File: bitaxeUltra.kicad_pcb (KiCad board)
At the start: 4 copper layers, 56.5 x 99.8 mm, 137 parts, among them J1 54-00164, J2 Conn_01x02, J3 Conn_01x05, J4 Conn_01x04, J5 TC2030-IDC, J7 Conn_01x02, J8 USB_C_Receptacle_USB2.0, J9 Conn_01x04, Q1 CSD17311Q5, Q2 CSD17311Q5, Q4 2N7002K, SW1 GT-TC029B-H025-L1N, SW2 GT-TC029B-H025-L1N, U1 25MHz, U10 DS4432U+, U11 RT9080-33GJ5, U12 ESP32-S3-WROOM-1, U14 BM1366_mode1, U2 TXB0104RGYR, U5 MCP1824T-1802E, U6 MCP1824T-0802E, U7 EMC2101, U8 INA260, U9 TPS40305, Y1 32.768kHz

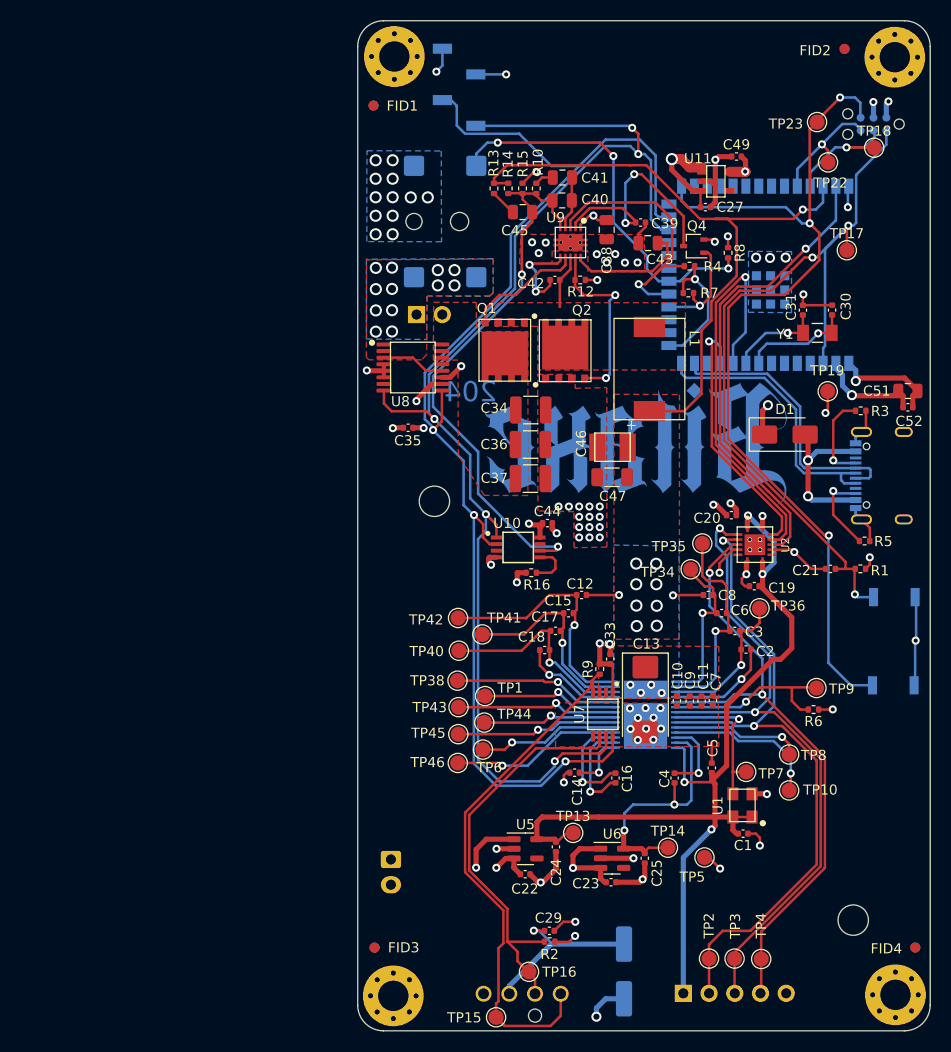
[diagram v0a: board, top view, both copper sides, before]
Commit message: Power analysis; updates to 205pd
Started analysis based on the 204 with an architecture diagram and with an smath document. Copied over manually changes from the 205 branch and started updating the schematic with USB PD capabilities. Only added decoy USB PD chip (CH224K), still need to fix power supplies.
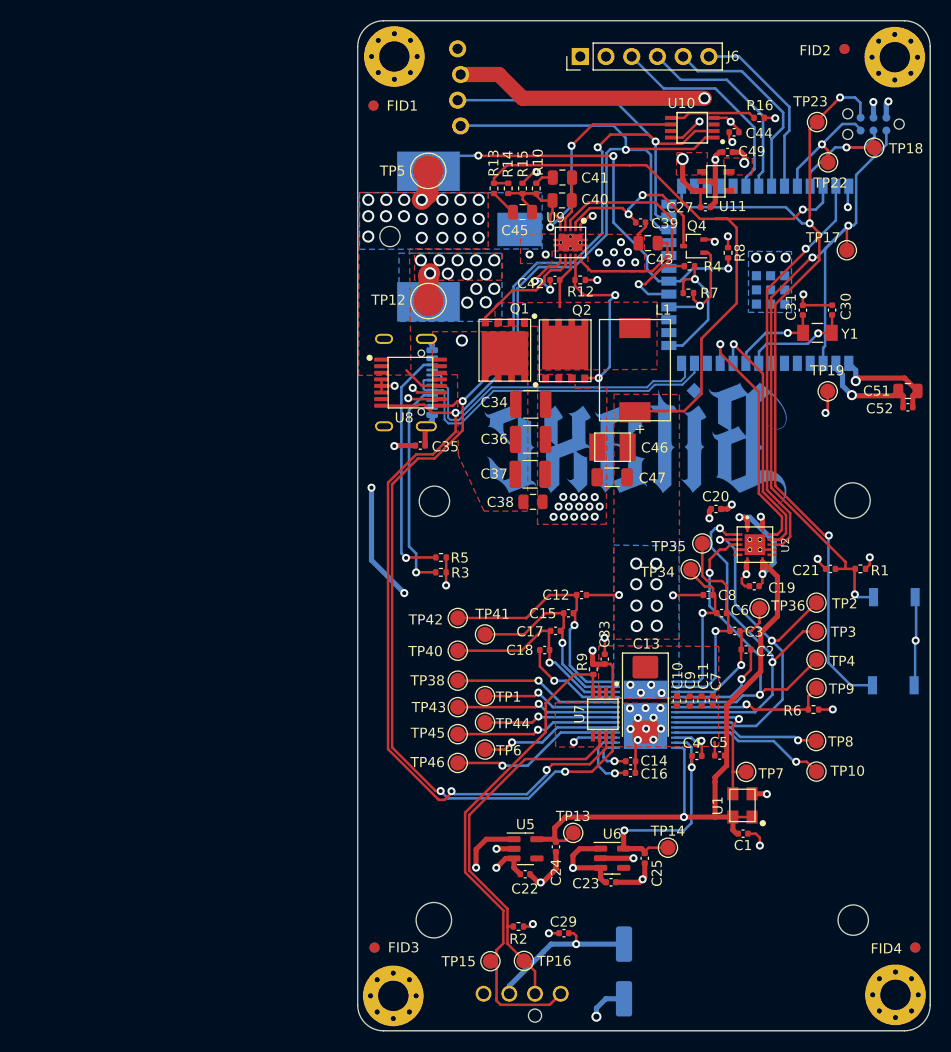
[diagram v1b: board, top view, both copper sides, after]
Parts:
- removed D1: SS310, Diode_SMD:D_SMA
- removed J2: Conn_01x02, bitaxe:JST_XH_B2B-XH-A_1x02_P2.50mm_Vertical
- removed J3: Conn_01x05, Connector_PinHeader_2.54mm:PinHeader_1x05_P2.54mm_Vertical
- removed J7: Conn_01x02, Connector_PinHeader_2.54mm:PinHeader_1x02_P2.54mm_Vertical
- added H1: MountingHole, MountingHole:MountingHole_3.5mm, F.Cu at (126.1, 94.9)
- added H2: MountingHole, MountingHole:MountingHole_3.5mm, F.Cu at (84.7, 136.4)
- added J6: Conn_01x06, Connector_PinHeader_2.54mm:PinHeader_1x06_P2.54mm_Vertical, F.Cu at (99.2, 51.1)
- added TP12: TestPoint, TestPoint:TestPoint_Pad_D3.0mm, F.Cu at (84.2, 75.2)
- J1: value 54-00164 -> PJ-036AH-SMT; footprint bitaxe:BarrelJack_Wuerth_694106106102_2.0x5.5mm -> Connector_BarrelJack:BarrelJack_CUI_PJ-036AH-SMT_Horizontal
- J9: footprint Connector_PinSocket_2.54mm:PinSocket_1x04_P2.54mm_Vertical_SMD_Pin1Right -> bitaxe:PinHeader_1x04_P2.54mm_Vertical_shifted
- TP5: footprint TestPoint:TestPoint_Pad_D1.5mm -> TestPoint:TestPoint_Pad_D3.0mm
- moved TP5 73.1 mm to (84.2, 62.4)
- moved R16 50.3 mm to (116.8, 57.1), turned to 0 degrees
- moved J8 50.0 mm to (80.9, 83.3), turned to 90 degrees
- moved U10 44.9 mm to (110.2, 58.1), turned to 180 degrees
- moved R3 44.4 mm to (85.4, 102.0)
- moved C44 42.8 mm to (114.4, 58.5)
- moved R5 41.9 mm to (85.4, 100.5)
- moved TP2 36.7 mm to (122.5, 105.0)
- moved TP3 33.3 mm to (122.5, 107.8)
- moved TP4 30.0 mm to (122.5, 110.7), turned to 0 degrees
- moved C38 27.8 mm to (94.5, 95.0), turned to 0 degrees
- moved C14 5.65 mm to (104.2, 120.7), turned to 0 degrees
- moved TP15 5.57 mm to (90.3, 140.4)
- moved U3 4.21 mm to (96.7, 71.6), turned to 180 degrees
- moved J9 3.80 mm to (87.2, 50.3)
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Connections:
- net Net-(U12-GPIO19/U1RTS/ADC2_CH8/CLK_OUT2/USB_D-) renamed /ESP32/USB_D-
- net Net-(U12-GPIO20/U1CTS/ADC2_CH9/CLK_OUT1/USB_D+) renamed /ESP32/USB_D+
- J8 pad A4: Net-(D1-Pad2) -> unconnected-(J8-VBUS-PadA4)
- J8 pad B4: Net-(D1-Pad2) -> unconnected-(J8-VBUS-PadB4)
- TP5 pad 1: GND -> /Power/VIN
- U12 pad 32: unconnected-(U12-MTCK/GPIO39/CLK_OUT3/SUBSPICS1-Pad32) -> Net-(J6-Pin_3)
- U12 pad 33: unconnected-(U12-MTDO/GPIO40/CLK_OUT2-Pad33) -> Net-(J6-Pin_4)
- U12 pad 34: unconnected-(U12-MTDI/GPIO41/CLK_OUT1-Pad34) -> Net-(J6-Pin_5)
- U12 pad 35: unconnected-(U12-MTMS/GPIO42-Pad35) -> Net-(J6-Pin_6)
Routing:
- net /BM1366/CI: track 67.5 -> 38.3 mm
- net /BM1366/RO: track 66.2 -> 37.6 mm
- net /BM1366/RST_N: track 62.1 -> 34.5 mm
- net /5V: track 217.6 -> 191.9 mm
- net /Power/OUT0: track 55.9 -> 31.2 mm
- net /3V3: track 74.3 -> 98.1 mm, vias 15 -> 18
- net Net-(J6-Pin_3): track 0.00 -> 21.2 mm
- net Net-(J6-Pin_4): track 0.00 -> 20.0 mm
- net Net-(J6-Pin_5): track 0.00 -> 19.9 mm
- net /BM1366/1V8: track 94.1 -> 74.9 mm, vias 4 -> 3
- net /SDA: track 128.0 -> 147.1 mm, vias 5 -> 4
- net GND: track 148.3 -> 129.7 mm, vias 83 -> 80
- net Net-(J6-Pin_6): track 0.00 -> 18.0 mm
- net /SCL: track 126.5 -> 143.3 mm, vias 3 -> 5
- net Net-(D1-Pad2): track 16.1 -> 0.00 mm, vias 2 -> 0
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- added copper zone on F.Cu, net /3V3
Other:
- board text added: "205"
- board text added: "5VDC"
- board text removed: "1V8"
- board text removed: "204"
- board text removed: "RST"
- board text removed: "RXI"
- board text removed: "TXO"

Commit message: SCH Draft 3, PCB Start
Finished some last minute changes to change 1V8 to 1V2 based on discord feedback. Updated level shifter and moved 25MHz oscillator to use 3V3 and be shifted down. Started working on layout.
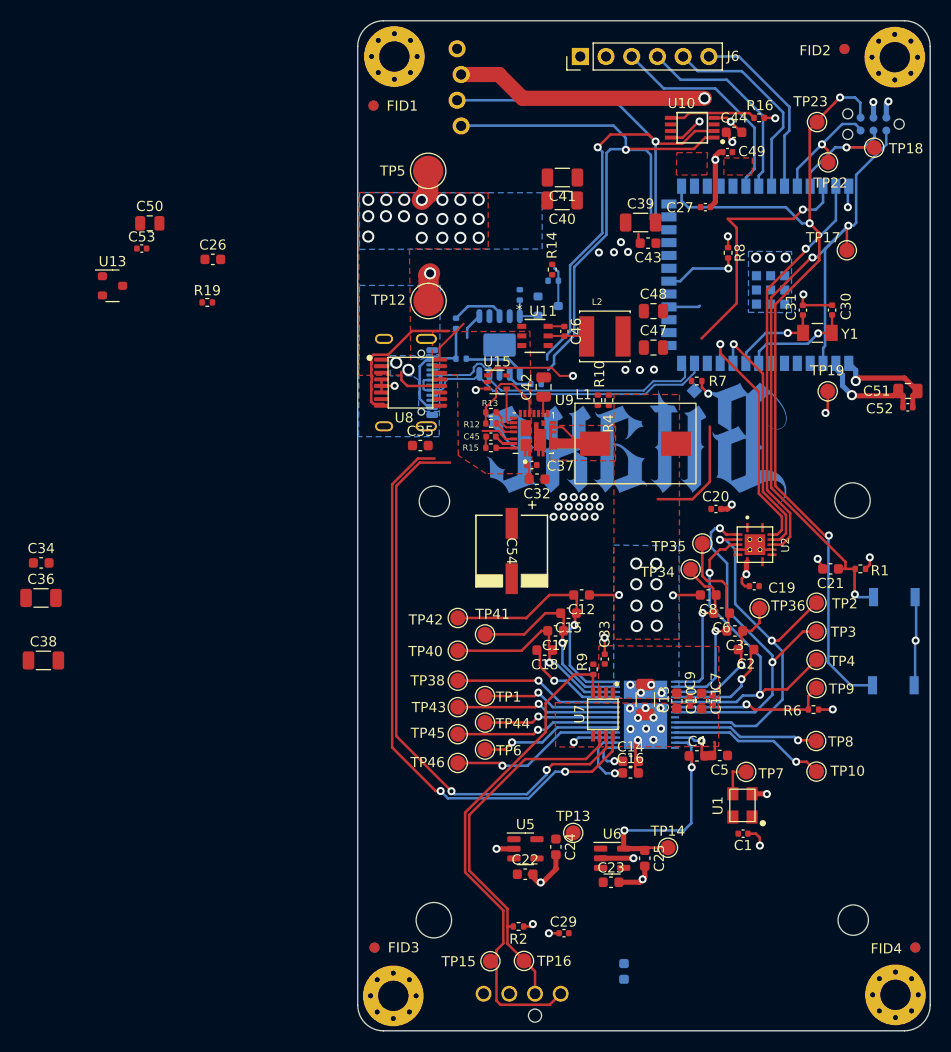
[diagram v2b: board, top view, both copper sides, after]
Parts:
- removed J1: PJ-036AH-SMT, Connector_BarrelJack:BarrelJack_CUI_PJ-036AH-SMT_Horizontal
- removed Q2: CSD17311Q5, bitaxe:CSD17311Q5
- removed Q4: 2N7002K, Package_TO_SOT_SMD:SOT-323_SC-70
- removed U3: ~, bitaxe:polarity
- added C26: 1uF, Capacitor_SMD:C_0603_1608Metric, F.Cu at (62.9, 71.1)
- added C32: 1uF, Capacitor_SMD:C_0603_1608Metric, F.Cu at (94.9, 92.8)
- added C48: 22uF, Capacitor_SMD:C_0805_2012Metric, F.Cu at (106.4, 76.2)
- added C50: 22uF, Capacitor_SMD:C_0805_2012Metric, F.Cu at (56.6, 67.5)
- added C53: 0.1uF, Capacitor_SMD:C_0402_1005Metric, F.Cu at (55.9, 70.0)
- added C54: 100uF, bitaxe:CAP_WCAP-ASLI_06p3X07p7_WRE, F.Cu at (92.4, 99.9)
- added L2: 6.8uH, bitaxe:IND_VLS5045EX-100M, F.Cu at (101.6, 78.7)
- added R11: 10k, Resistor_SMD:R_0402_1005Metric, B.Cu at (93.2, 74.6)
- added R17: 24k, Resistor_SMD:R_0402_1005Metric, B.Cu at (94.8, 83.4)
- added R18: 10k, Resistor_SMD:R_0402_1005Metric, B.Cu at (96.5, 73.2)
- added R19: 10k, Resistor_SMD:R_0402_1005Metric, F.Cu at (62.3, 75.3)
- added U13: AP7375-50SA-7, bitaxe:DIODESINC_SOT-23, F.Cu at (53.0, 73.7)
- added U15: 74LVC1G08, Package_TO_SOT_SMD:SOT-353_SC-70-5, F.Cu at (91.0, 83.2)
- added U4: CH224K, IC:ESSOP-10, B.Cu at (91.2, 79.5)
- C10, C11, C12, C14, C15, C16, C17, C18, C2, C21, C22, C23, C24, C25, C3, C35, C4, C44, C5, C6, C8: footprint Capacitor_SMD:C_0402_1005Metric -> Capacitor_SMD:C_0603_1608Metric
- C13: value 330uF -> 100uF; footprint Capacitor_Tantalum_SMD:CP_EIA-7343-31_Kemet-D_Pad2.25x2.55mm_HandSolder -> Capacitor_SMD:C_1206_3216Metric
- C27, C49: value 1uF -> 0.1uF
- C28: value 220uF -> 1uF; footprint Capacitor_SMD:CP_Elec_6.3x7.7 -> Capacitor_SMD:C_0603_1608Metric
- C34: value 47uF -> 1uF; footprint Capacitor_SMD:C_1210_3225Metric -> Capacitor_SMD:C_0603_1608Metric
- C36: value 47uF -> 100uF; footprint Capacitor_SMD:C_1210_3225Metric -> Capacitor_SMD:C_1206_3216Metric
- C37: value 47uF -> 0.1uF; footprint Capacitor_SMD:C_1210_3225Metric -> Capacitor_SMD:C_0402_1005Metric
- C38: value 1uF -> 100uF; footprint Capacitor_SMD:C_0805_2012Metric -> Capacitor_SMD:C_1206_3216Metric
- C39: value 3.3nF -> 100uF; footprint Capacitor_SMD:C_0402_1005Metric -> Capacitor_SMD:C_1206_3216Metric
- C40: value 180pF -> 100uF; footprint Capacitor_SMD:C_0805_2012Metric -> Capacitor_SMD:C_1206_3216Metric
- C41: value 1.5nF -> 100uF; footprint Capacitor_SMD:C_0805_2012Metric -> Capacitor_SMD:C_1206_3216Metric
- C42: value 0.1uF -> 4.7uF; footprint Capacitor_SMD:C_0402_1005Metric -> Capacitor_SMD:C_0805_2012Metric
- C43: value 10uF -> 1uF; footprint Capacitor_SMD:C_0805_2012Metric -> Capacitor_SMD:C_0603_1608Metric
- C45: value 470pF -> 0.1uF; footprint Capacitor_SMD:C_0805_2012Metric -> Capacitor_SMD:C_0402_1005Metric
- C46: value 220uF -> 0.1uF; footprint bitaxe:CAP_2R5TPE220MAFB -> Capacitor_SMD:C_0402_1005Metric
- C47: value 100uF -> 22uF; footprint Capacitor_SMD:C_1206_3216Metric -> Capacitor_SMD:C_0805_2012Metric
- L1: value 150nH -> 300nH; footprint bitaxe:FP1005R1-R15-R -> bitaxe:INDUCTOR_SPB1007-R30M
- Q1: value CSD17311Q5 -> DMP31D1U-7; footprint bitaxe:CSD17311Q5 -> bitaxe:DIODESINC_SOT-23; moved to B.Cu
- R10: value 3.83k -> 10k
- R12: value 4.12k -> 100k
- R13: value 1.33k -> 499k
- R14: value 4.99k -> 10k
- R15: value 3.32k -> 1
- R3: value 5.1k -> 10k; moved to B.Cu
- R4: value 10k -> 9.53k
- R5: value 5.1k -> 1k; moved to B.Cu
- U11: value RT9080-33GJ5 -> AP63203QWU-7; footprint bitaxe:RT9080-33GJ5 -> bitaxe:TSOT26_DIO
- U5: value MCP1824T-1802E -> MCP1824T-1202E/OT
- U9: value TPS40305 -> SIC431AED-T1-GE3; footprint bitaxe:TPS40305 -> bitaxe:REGULATOR_SIC431AED-T1-GE3
- moved C36 50.8 mm to (45.9, 104.5)
- moved C34 50.8 mm to (45.9, 101.1)
- moved C38 50.8 mm to (46.1, 110.7)
- moved R15 25.8 mm to (90.3, 89.7), turned to 180 degrees
- moved R3 24.6 mm to (86.9, 77.4), turned to 90 degrees
- moved U11 23.5 mm to (94.7, 78.6)
- moved C45 22.4 mm to (90.3, 88.6), turned to 180 degrees
- moved R13 22.1 mm to (90.3, 86.2), turned to 180 degrees
- moved R10 21.8 mm to (100.9, 85.0)
- moved R5 19.7 mm to (87.4, 80.9)
- moved U9 19.2 mm to (94.5, 88.2), turned to 90 degrees
- moved R12 16.7 mm to (90.3, 87.3)
- moved R4 15.4 mm to (102.0, 85.0), turned to 90 degrees
- moved C47 13.4 mm to (106.4, 79.8), turned to 0 degrees
- moved C46 12.4 mm to (97.6, 78.2), turned to -90 degrees
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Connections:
- net /BM1366/0V8 renamed +0V8
- net /ESP32/USB_D+ renamed /USB_D+
- net /ESP32/USB_D- renamed /USB_D-
- net /Fan/FAN_PWM renamed /Fan and Screen/FAN_PWM
- net /Fan/FAN_TACH renamed /Fan and Screen/FAN_TACH
- net /PLUG_SENSE renamed /ESP32/PLUG_SENSE
- C1 pad 2: /BM1366/1V8 -> +3.3V
- C19 pad 1: /BM1366/1V8 -> +1V2
- C20 pad 1: /3V3 -> +3.3V
- C22 pad 1: /5V -> +3V3
- C23 pad 1: /5V -> +3V3
- C24 pad 1: /BM1366/1V8 -> +1V2
- C27 pad 1: /5V -> +12V
- C28 pad 1: /5V -> +12V
- C29 pad 1: /5V -> +12V
- C33 pad 1: /3V3 -> +3V3
- C34 pad 1: /5V -> GND
- C34 pad 2: GND -> +12V
- C35 pad 1: /3V3 -> GND
- C35 pad 2: GND -> +3V3
- C36 pad 1: /5V -> /VDD
- C37 pad 1: /5V -> +12V
- C38 pad 1: /5V -> /VDD
- C39 pad 1: Net-(Q4-D) -> /VDD
- C40 pad 1: Net-(U9-COMP) -> /VDD
- C40 pad 2: /Power/OUT0 -> GND
- C41 pad 1: Net-(U9-COMP) -> /VDD
- C41 pad 2: Net-(C41-Pad2) -> GND
- C42 pad 1: Net-(U9-BOOT) -> Net-(U9-VDRV)
- C42 pad 2: /Power/SW -> GND
- C43 pad 1: Net-(U9-BP) -> /Power/VOUT_INTERNAL
- C44 pad 1: /3V3 -> +3V3
- C45 pad 1: Net-(C45-Pad1) -> Net-(U9-BOOT)
- C45 pad 2: /Power/OUT0 -> Net-(C45-Pad2)
- C46 pad 1: /VDD -> Net-(U11-BST)
- C46 pad 2: GND -> Net-(U11-SW)
- C47 pad 1: /VDD -> +3V3
- C49 pad 1: /3V3 -> +12V
- C5 pad 1: /BM1366/1V8 -> +1V2
- C51 pad 1: /3V3 -> +3V3
- C52 pad 1: /3V3 -> +3V3
- J4 pad 2: /5V -> +12V
- J5 pad 2: /3V3 -> +3V3
- J6 pad 1: /5V -> +5V
- J8 pad A4: unconnected-(J8-VBUS-PadA4) -> IN+
- J8 pad B4: unconnected-(J8-VBUS-PadB4) -> IN+
- J9 pad 2: /3V3 -> +3V3
- L1 pad 1: /Power/SW -> Net-(L1-Pad1)
- Q1 pad 1: /Power/SW -> /Power/USB_PG
- Q1 pad 2: /Power/SW -> +3V3
- Q1 pad 3: /Power/SW -> Net-(Q1-D)
- R1 pad 1: /3V3 -> +3V3
- R10 pad 1: Net-(C41-Pad2) -> /Power/VDD_FB
- R10 pad 2: /Power/OUT0 -> GND
- R12 pad 1: Net-(Q2-G) -> /Power/VOUT_INTERNAL
- R12 pad 2: GND -> Net-(U9-MODE1)
- R13 pad 1: /VDD -> Net-(U9-MODE2)
- R13 pad 2: Net-(C45-Pad1) -> /Power/VOUT_INTERNAL
- R14 pad 1: /VDD -> +3V3
- R14 pad 2: /Power/OUT0 -> /ESP32/PGOOD
- R15 pad 1: /Power/OUT0 -> Net-(U9-PHASE)
- R15 pad 2: GND -> Net-(C45-Pad2)
- R2 pad 2: /3V3 -> +3V3
- R3 pad 1: GND -> IN+
- R3 pad 2: Net-(J8-CC1) -> Net-(U4-VBUS)
- R4 pad 1: /3V3 -> /VDD
- R4 pad 2: /Power/PGOOD -> /Power/VDD_FB
- R5 pad 1: GND -> Net-(U4-VDD)
- R5 pad 2: Net-(J8-CC2) -> IN+
- R7 pad 1: /3V3 -> +3V3
- R8 pad 1: /3V3 -> +3V3
- R9 pad 2: /3V3 -> +5V
- TP13 pad 1: /BM1366/1V8 -> +1V2
- TP19 pad 1: /3V3 -> +3V3
- TP5 pad 1: /Power/VIN -> IN+
- U1 pad 1: /BM1366/1V8 -> Net-(U1-EN)
- U1 pad 3: /BM1366/CLKI -> /BM1366/CLKI_HI
- U1 pad 4: /BM1366/1V8 -> +3.3V
- U10 pad 6: /Power/OUT0 -> /Power/VDD_FB
- U10 pad 7: /Power/OUT1 -> unconnected-(U10-OUT1-Pad7)
- U10 pad 8: /3V3 -> +3V3
- U11 pad 1: /5V -> +3V3
- U11 pad 2: GND -> +12V
- U11 pad 3: /5V -> +12V
- U11 pad 4: unconnected-(U11-NC-Pad4) -> GND
- U11 pad 5: /3V3 -> Net-(U11-SW)
- U12 pad 15: /3V3 -> +3V3
- U12 pad 19: /Power/PGOOD -> /ESP32/PGOOD
- U12 pad 2: /3V3 -> +3V3
- U14 pad 14: /BM1366/1V8 -> +1V2
- U2 pad 1: /BM1366/1V8 -> +1V8
- U2 pad 14: /3V3 -> +3.3V
- U2 pad 8: /BM1366/1V8 -> +1V8
- U5 pad 1: /5V -> +3V3
- U5 pad 3: /5V -> /Power/ASIC_EN
- U5 pad 5: /BM1366/1V8 -> +1V2
- U6 pad 1: /5V -> +3V3
- U6 pad 3: /5V -> /Power/ASIC_EN
- U7 pad 1: /3V3 -> +3V3
- U8 pad 1: /Power/VIN -> IN+
- U8 pad 10: /3V3 -> +3V3
- U8 pad 12: /Power/VIN -> IN+
- U8 pad 14: /5V -> +12V
- U8 pad 15: /5V -> +12V
- U8 pad 16: /5V -> +12V
- U8 pad 2: /Power/VIN -> IN+
- U8 pad 3: /Power/VIN -> IN+
- U9 pad 1: /5V -> +12V
- U9 pad 10: Net-(U9-BP) -> unconnected-(U9-GL-Pad10)
- U9 pad 11: GND -> unconnected-(U9-GL-Pad10)
- U9 pad 2: Net-(Q4-D) -> +12V
- U9 pad 3: /Power/PGOOD -> GND
- U9 pad 4: Net-(U9-COMP) -> GND
- U9 pad 5: /Power/OUT0 -> Net-(L1-Pad1)
- U9 pad 6: Net-(U9-BOOT) -> Net-(L1-Pad1)
- U9 pad 7: Net-(Q1-G) -> Net-(L1-Pad1)
- U9 pad 8: /Power/SW -> Net-(L1-Pad1)
- U9 pad 9: Net-(Q2-G) -> Net-(L1-Pad1)
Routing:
- net /5V: track 191.9 -> 0.00 mm, vias 7 -> 0
- net /3V3: track 98.1 -> 0.00 mm, vias 18 -> 0
- net /BM1366/1V8: track 74.9 -> 0.00 mm, vias 3 -> 0
- net +3V3: track 0.00 -> 47.4 mm, vias 0 -> 9
- net /ESP32/PLUG_SENSE: track 41.0 -> 7.44 mm, vias 3 -> 1
- net /Power/OUT0: track 31.2 -> 0.00 mm, vias 2 -> 0
- net /VDD: track 71.5 -> 42.5 mm
- net /Power/PGOOD: track 27.2 -> 0.00 mm, vias 1 -> 0
- net Net-(J8-CC2): track 24.0 -> 0.00 mm, vias 1 -> 0
- net GND: track 129.7 -> 109.7 mm, vias 80 -> 61
- net IN+: track 0.00 -> 19.6 mm, vias 0 -> 21
- net /SCL: track 143.3 -> 124.4 mm, vias 5 -> 4
- net Net-(J8-CC1): track 21.2 -> 2.64 mm, vias 1 -> 0
- net Net-(Q4-D): track 18.1 -> 0.00 mm, vias 2 -> 0
- net Net-(Q2-G): track 17.5 -> 0.00 mm, vias 2 -> 0
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- added copper zone on F.Cu, net +12V
- added copper zone on F.Cu, net +3V3
- added copper zone on In2.Cu, net +3V3
- added copper zone on B.Cu, net IN+
- added copper zone on F.Cu, net IN+
- added copper zone on F.Cu, net Net-(L1-Pad1)
- removed copper zone on F.Cu, net /3V3
- removed copper zone on In2.Cu, net /3V3
- removed copper zone on F.Cu, net /5V
- removed copper zone on F.Cu, net /Power/SW
- removed copper zone on B.Cu, net /Power/VIN
- removed copper zone on F.Cu, net /Power/VIN
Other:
- board text removed: "5VDC"

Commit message: PCB Work
Parts now all within board but various issues still exist. Routing started, placement needs to be refined.
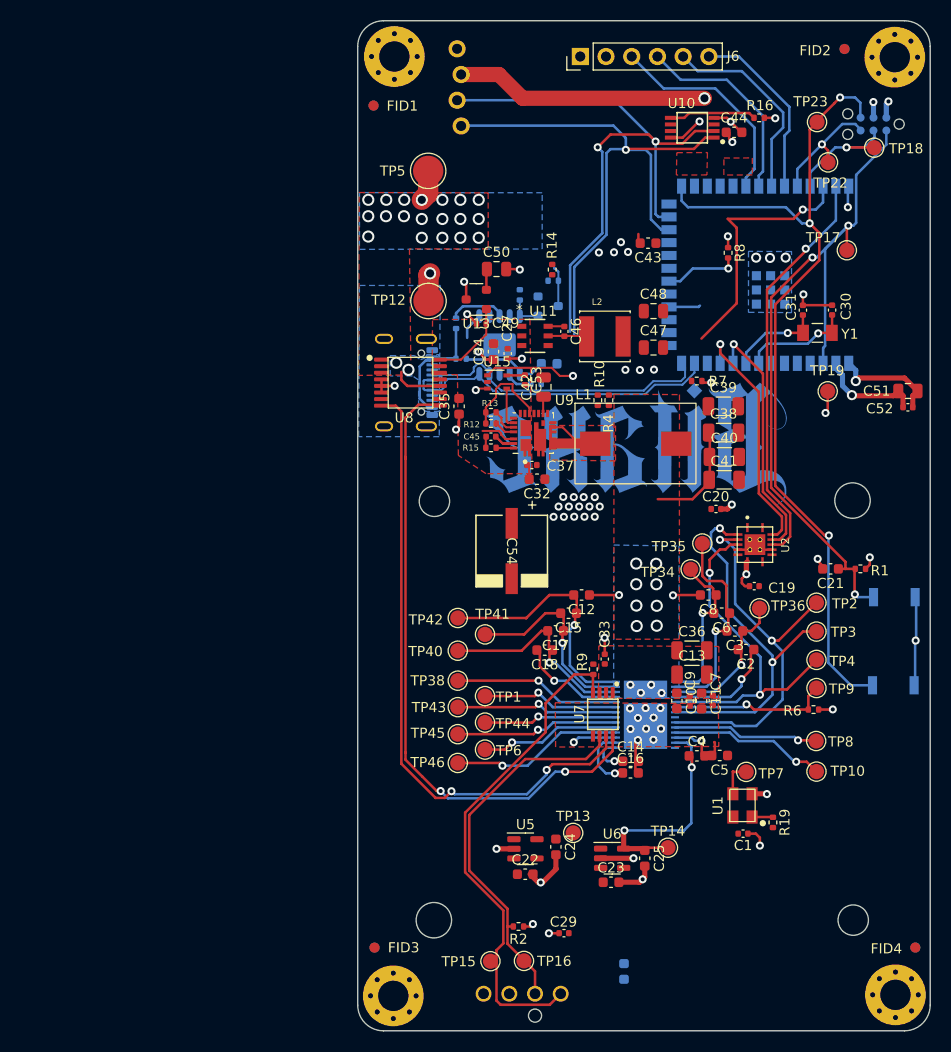
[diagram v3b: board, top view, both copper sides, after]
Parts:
- C26: moved to B.Cu
- moved R19 75.9 mm to (118.2, 126.7), turned to -90 degrees
- moved C38 70.8 mm to (113.3, 88.2)
- moved C36 64.5 mm to (110.2, 109.7)
- moved C34 49.3 mm to (90.6, 80.2), turned to 90 degrees
- moved C53 40.0 mm to (93.7, 83.0), turned to -90 degrees
- moved U13 36.0 mm to (88.9, 75.0), turned to 180 degrees
- moved C26 34.8 mm to (96.1, 81.4)
- moved C50 34.5 mm to (90.9, 72.0)
- moved C41 33.9 mm to (113.4, 92.9), turned to 0 degrees
- moved C40 30.0 mm to (113.4, 90.6), turned to 0 degrees
- moved C49 29.6 mm to (89.4, 77.5)
- moved C27 24.3 mm to (92.0, 80.4), turned to -90 degrees
- moved C39 19.9 mm to (113.3, 85.6)
- moved C35 5.45 mm to (87.2, 85.6), turned to 90 degrees
- moved C13 5.22 mm to (110.2, 112.1), turned to 0 degrees
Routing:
- net /SDA: track 136.9 -> 122.5 mm
- net +12V: track 9.52 -> 13.1 mm
- net GND: track 109.7 -> 112.9 mm, vias 61 -> 66
- net Net-(U4-VDD): track 6.12 -> 8.66 mm
- net +5V: track 0.00 -> 2.07 mm
- net Net-(U1-EN): track 0.00 -> 2.07 mm
- net +3V3: track 47.4 -> 49.3 mm
- net /SCL: track 124.4 -> 125.5 mm
- net /ESP32/PWR_EN: track 4.62 -> 4.10 mm
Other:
- board text added: "205pd"
- board text removed: "205"
